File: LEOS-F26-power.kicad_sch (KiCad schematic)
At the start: 1 part

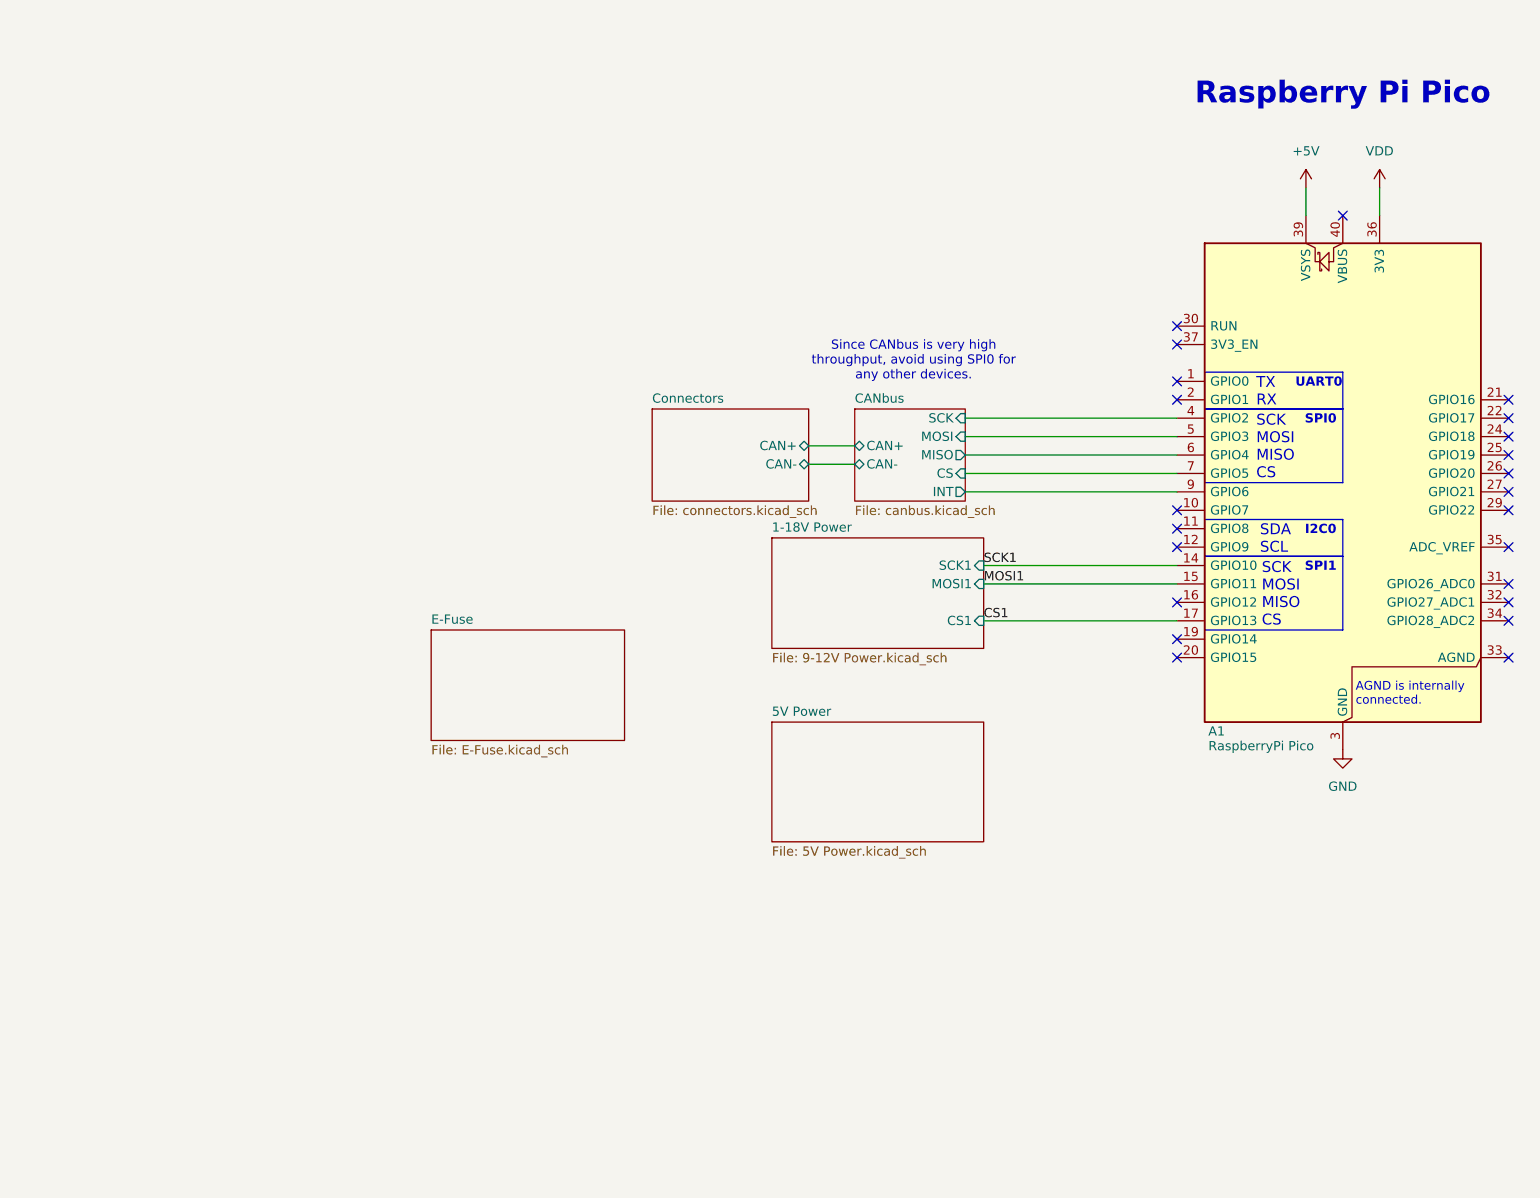
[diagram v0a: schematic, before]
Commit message: Rename references, update symbols and schematic layout
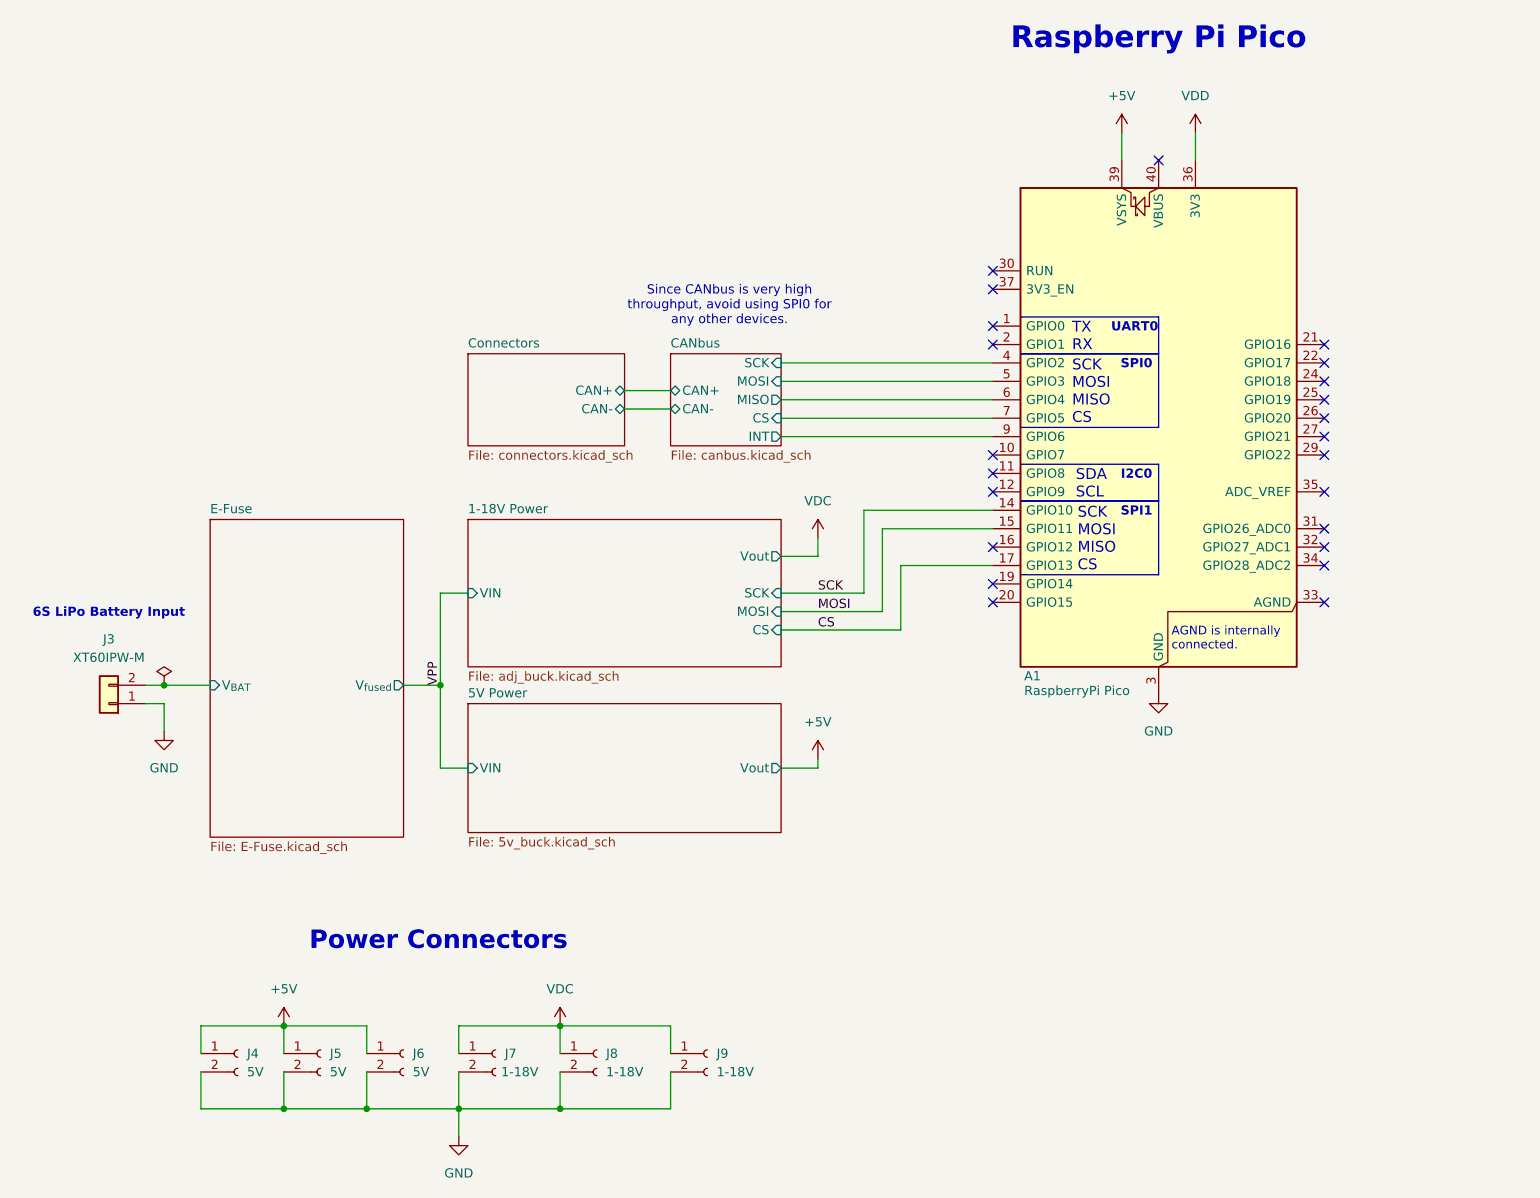
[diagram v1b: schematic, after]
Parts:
- added J3: XT60IPW-M, LEOS:AMASS_XT60IPW-M_1x03_P7.20mm_Horizontal, symbol Connector_Generic:Conn_01x02
- added J4, J5, J6: 5V, Connector_JST:JST_XH_S2B-XH-A_1x02_P2.50mm_Horizontal, symbol Connector:Conn_01x02_Socket
- added J7, J8, J9: 1-18V, Connector_JST:JST_XH_S2B-XH-A_1x02_P2.50mm_Horizontal, symbol Connector:Conn_01x02_Socket
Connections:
- net +5V: now also J4.1 (Pin_1), J5.1 (Pin_1), J6.1 (Pin_1)
- net GND: now also J3.1 (Pin_1), J4.2 (Pin_2), J5.2 (Pin_2), J6.2 (Pin_2), J7.2 (Pin_2), J8.2 (Pin_2), J9.2 (Pin_2)
- net CS1 renamed CS
- net MOSI1 renamed MOSI
- net SCK1 renamed SCK
- new net E-Fuse/V_{BAT}: J3.2 (Pin_2)
- new net VDC: J7.1 (Pin_1), J8.1 (Pin_1), J9.1 (Pin_1)
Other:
- sheet 1-18V Power: file 9-12V Power.kicad_sch -> adj_buck.kicad_sch
- sheet 1-18V Power ports: added CS, MOSI, SCK, VIN, Vout; removed CS1, MOSI1, SCK1
- sheet 5V Power: file 5V Power.kicad_sch -> 5v_buck.kicad_sch
- sheet 5V Power ports: added VIN, Vout; removed none
- sheet E-Fuse ports: added V_{BAT}, V_{fused}; removed none
- note added: "6S LiPo Battery Input"
- note added: "Power Connectors"
- moved on the sheet: A1
